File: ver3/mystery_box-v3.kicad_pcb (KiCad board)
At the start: 2 copper layers, 136 x 100 mm, 61 parts, among them J1 Screw_Terminal_01x02, J10 Screw_Terminal_01x02, J11 Screw_Terminal_01x02, J12 Screw_Terminal_01x02, J13 Screw_Terminal_01x02, J14 Screw_Terminal_01x02, J15 Screw_Terminal_01x02, J16 Screw_Terminal_01x02, J17 Screw_Terminal_01x02, J18 Barrel_Jack_MountingPin, J20 rj45-CC-X2-Aliexpress, J3 SERIAL1, J8 Screw_Terminal_01x02, J9 Screw_Terminal_01x02, Q1 IRLZ44N, Q2 IRLZ44N, Q3 IRLZ44N, SW01 Screw_Terminal_01x02, SW02 Screw_Terminal_01x02, SW03 Screw_Terminal_01x02, U1 THVD1400D

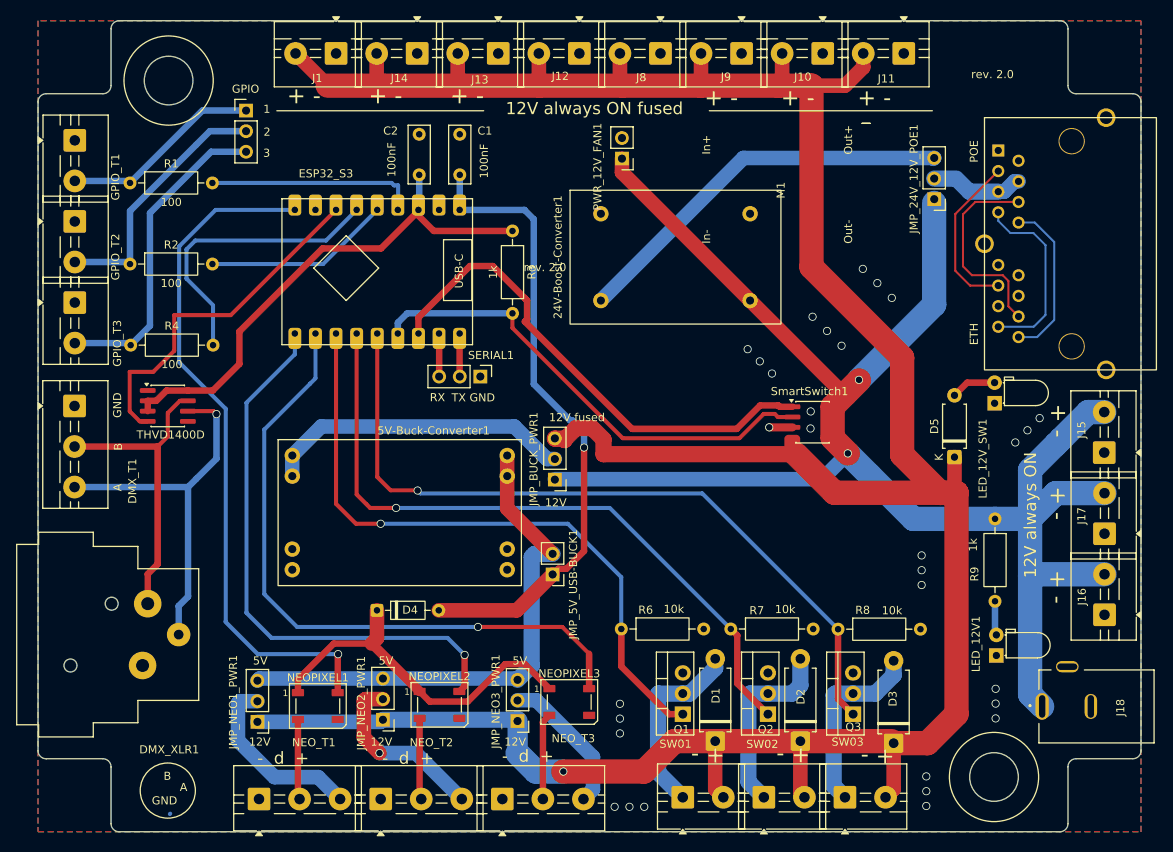
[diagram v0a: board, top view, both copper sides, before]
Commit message: ver3: moved boost converter to designated place
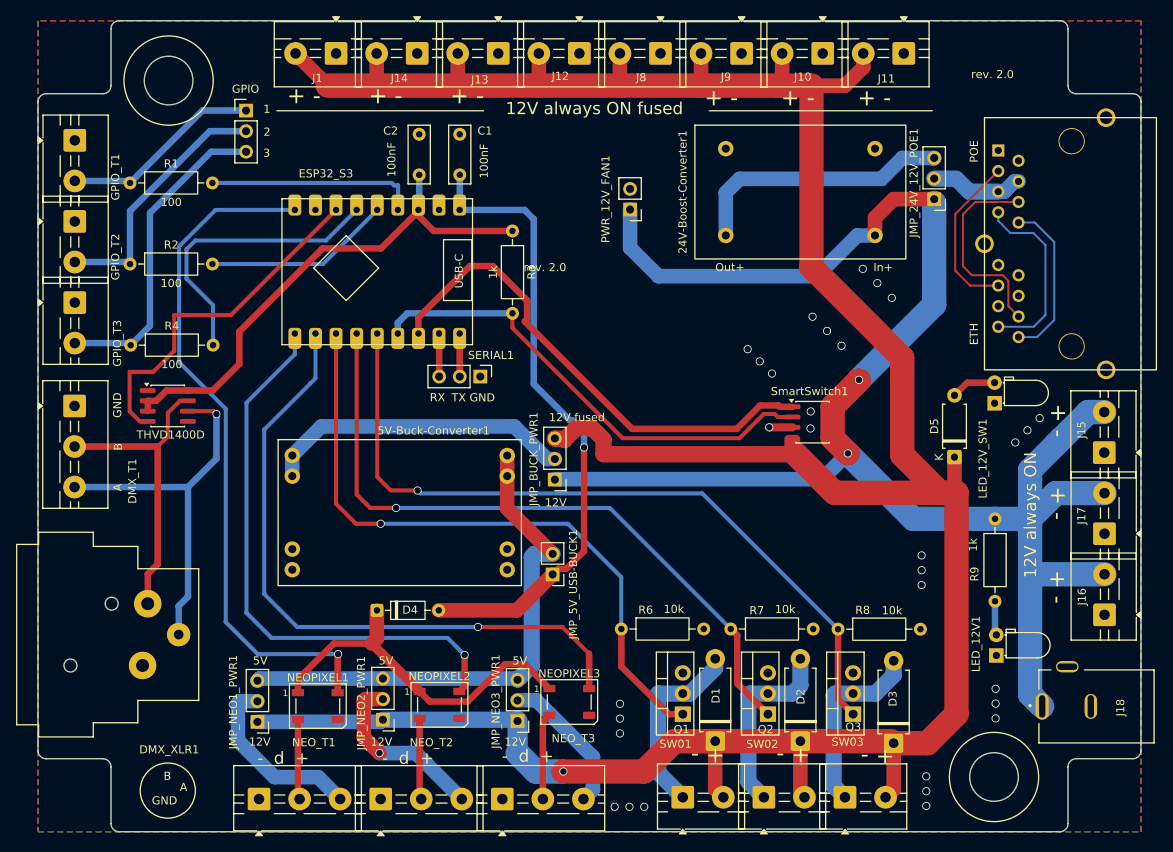
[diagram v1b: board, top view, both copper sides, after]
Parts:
- moved 24V-Boost-Converter1 17.4 mm to (231.5, 46.1)
- moved PWR_12V_FAN1 6.35 mm to (210.5, 48.3)
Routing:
- net VCC 24V: track 48.5 -> 32.9 mm
- net VCC 12V: track 203.0 -> 211.5 mm
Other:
- board text removed: "In-"
- board text removed: "Out-"

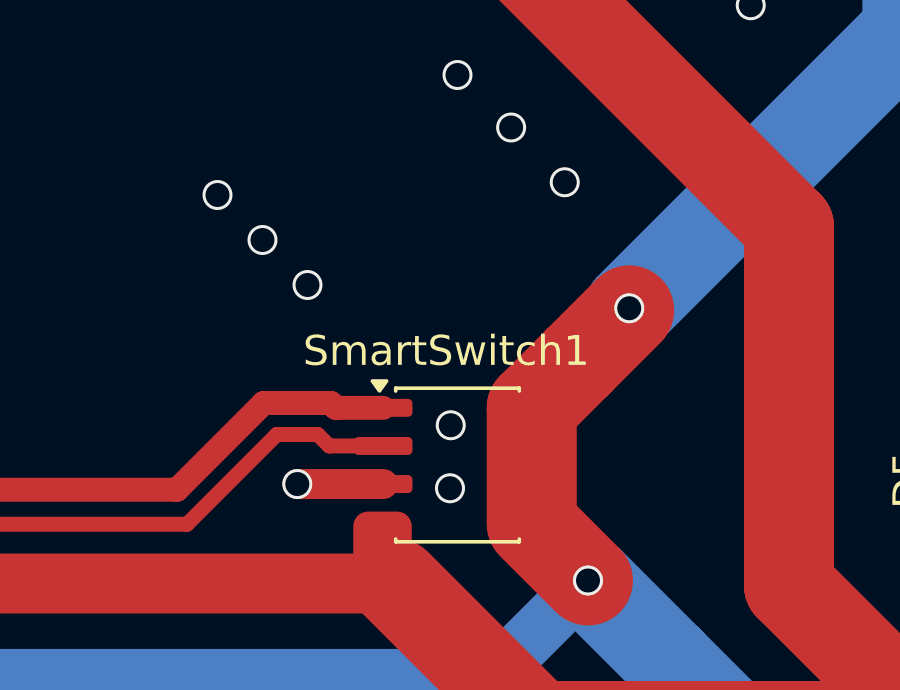
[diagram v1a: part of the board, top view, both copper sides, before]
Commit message: ver3: minor fixups of vias
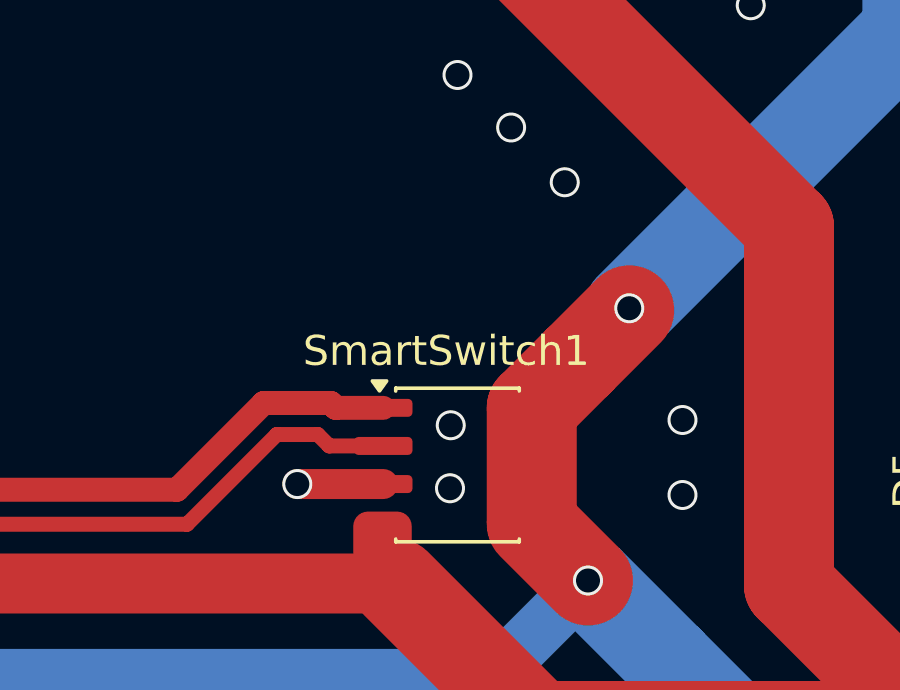
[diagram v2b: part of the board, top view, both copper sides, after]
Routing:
- net GND: vias 30 -> 29
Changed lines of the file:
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@@
 	)
 	(via
-		(at 228 68.5)
+		(at 240.5 73)
 		(size 1)
 		(drill 0.8)
@@
 	)
 	(via
-		(at 226.5 67)
+		(at 240.5 75.5)
 		(size 1)
 		(drill 0.8)
@@
 		(net "GND")
 	)
-	(via
-		(at 225 65.5)
-		(size 1)
-		(drill 0.8)
-		(layers "F.Cu" "B.Cu")
-		(free yes)
-		(net "GND")
-	)

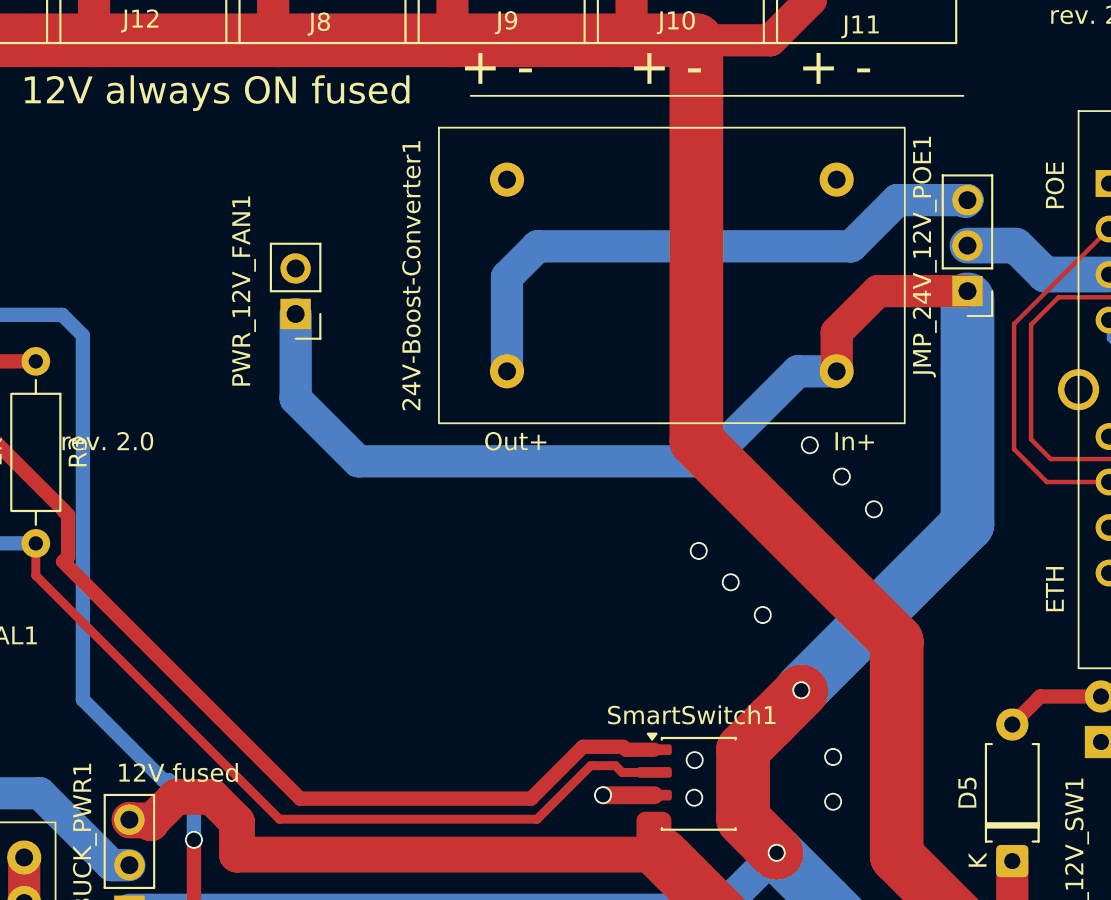
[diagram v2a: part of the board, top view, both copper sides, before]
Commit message: ver3: better POE JMP hints
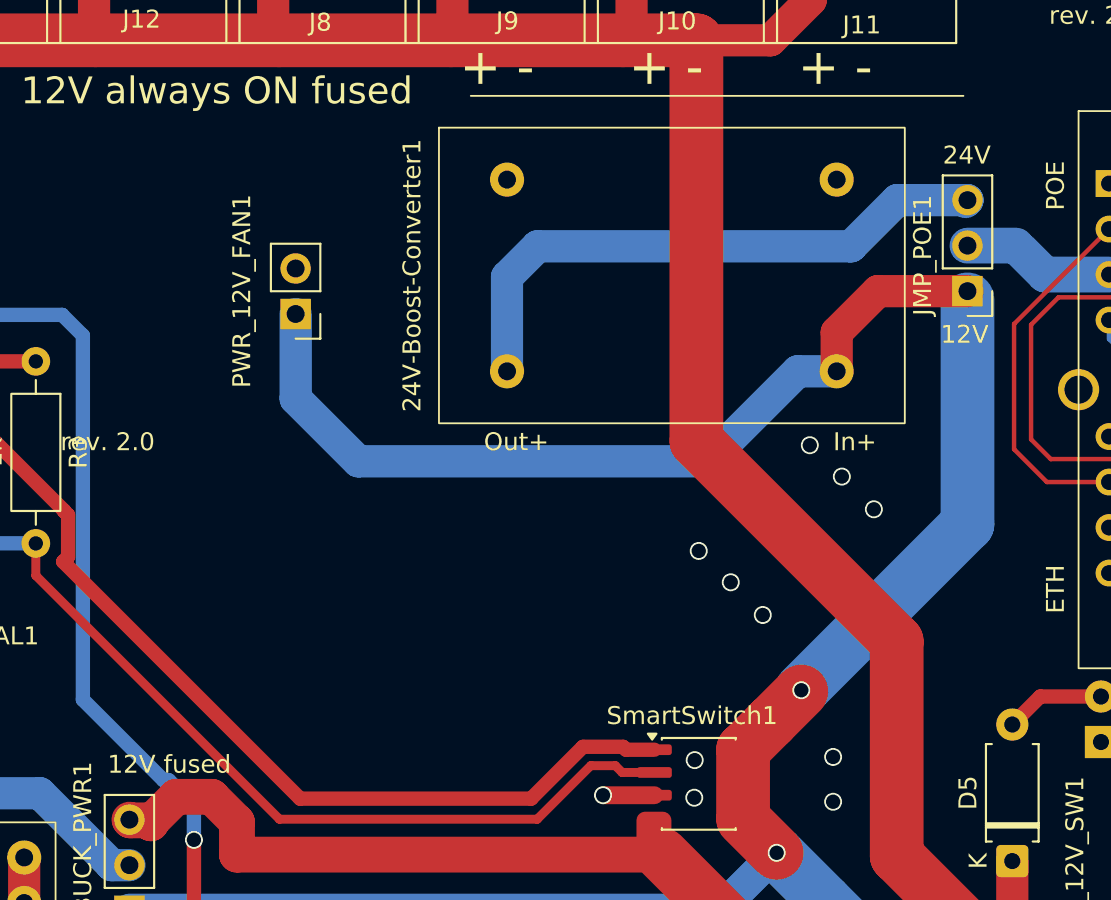
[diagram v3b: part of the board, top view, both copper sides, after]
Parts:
- renumbered JMP_24V_12V_POE1 to JMP_POE1
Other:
- board text added: "24V"
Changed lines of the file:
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@@
 		(descr "Through hole straight pin header, 1x03, 2.54mm pitch, single row")
 		(tags "Through hole pin header THT 1x03 2.54mm single row")
-		(property "Reference" "JMP_24V_12V_POE1"
+		(property "Reference" "JMP_POE1"
 			(at 2.5 2 90)
 			(layer "F.SilkS")
@@
 		)
 	)
-	(gr_text "12V"
-		(at 200 85 0)
+	(gr_text "12V fused"
+		(at 200 74 0)
 		(layer "F.SilkS")
 		(effects
@@
 		)
 	)
-	(gr_text "12V fused"
-		(at 200.5 74.5 0)
+	(gr_text "12V"
+		(at 200 85 0)
 		(layer "F.SilkS")
 		(effects
@@
 		(layer "F.SilkS")
 		(effects
+			(font
+				(size 1 1)
+				(thickness 0.1)
+			)
+			(justify left bottom)
+		)
+	)
+	(gr_text "12V"
+		(at 246.5 50 0)
+		(layer "F.SilkS")
+		(effects
+			(font
+				(size 1 1)
+				(thickness 0.1)
+			)
+			(justify left bottom)
+		)
+	)
+	(gr_text "24V"
+		(at 246.62 40 0)
+		(layer "F.SilkS")
+		(effects
